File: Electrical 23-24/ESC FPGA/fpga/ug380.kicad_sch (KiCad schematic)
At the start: 0 parts

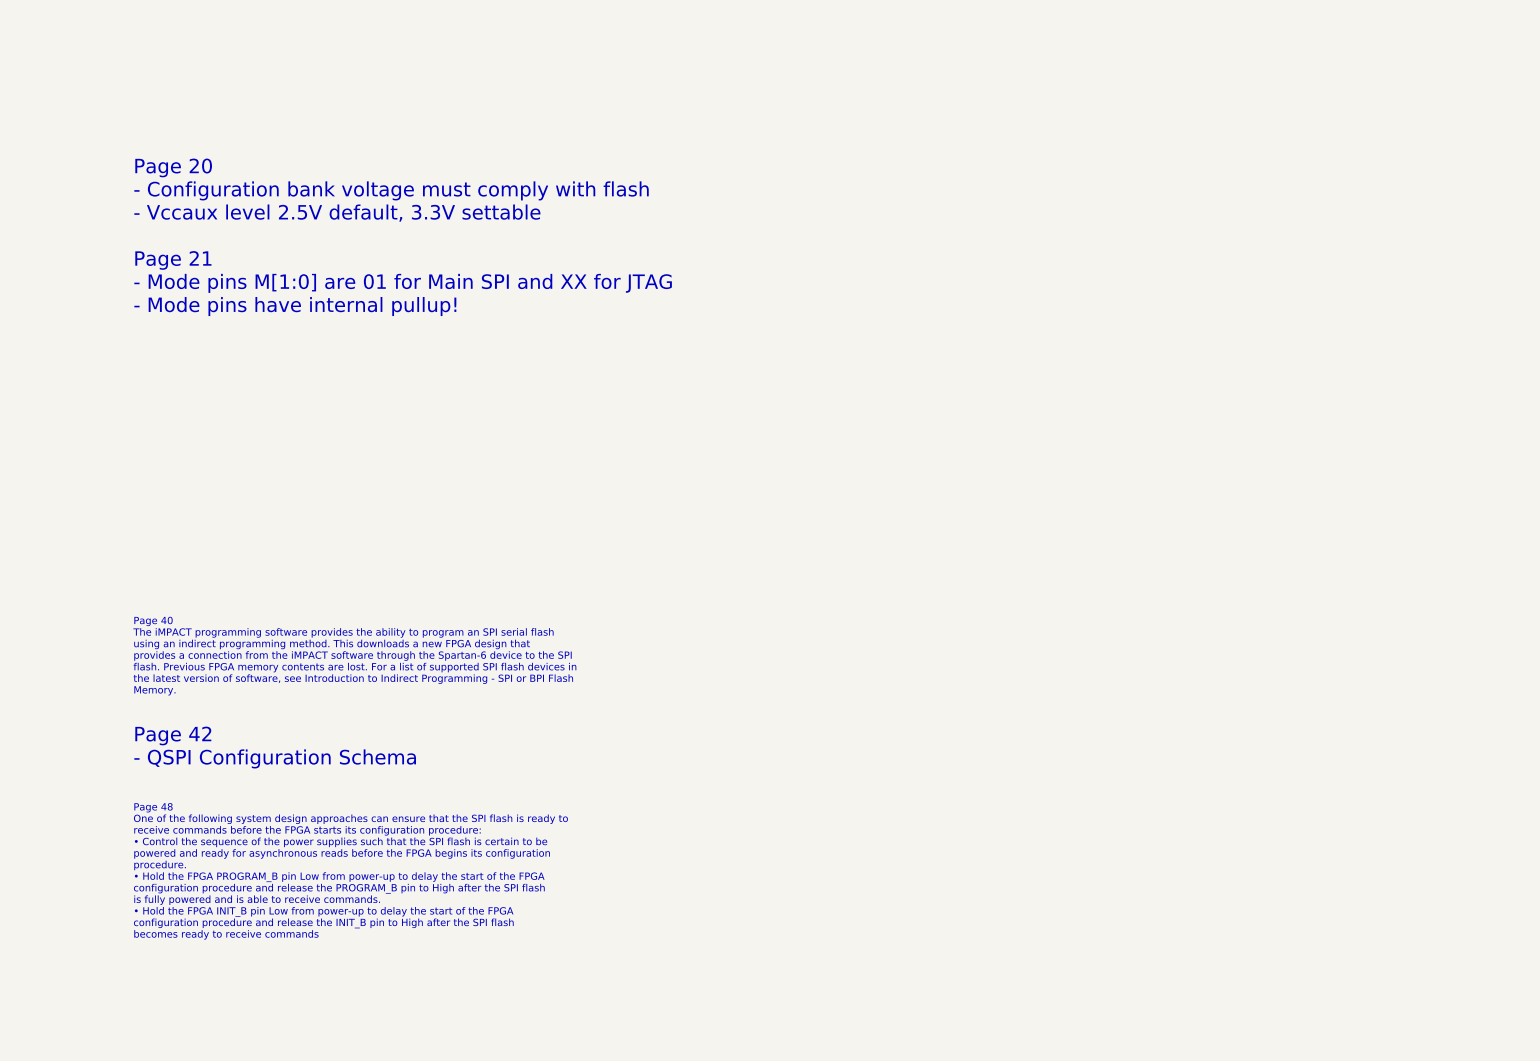
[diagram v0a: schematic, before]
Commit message: Finish programming interface with FPGA
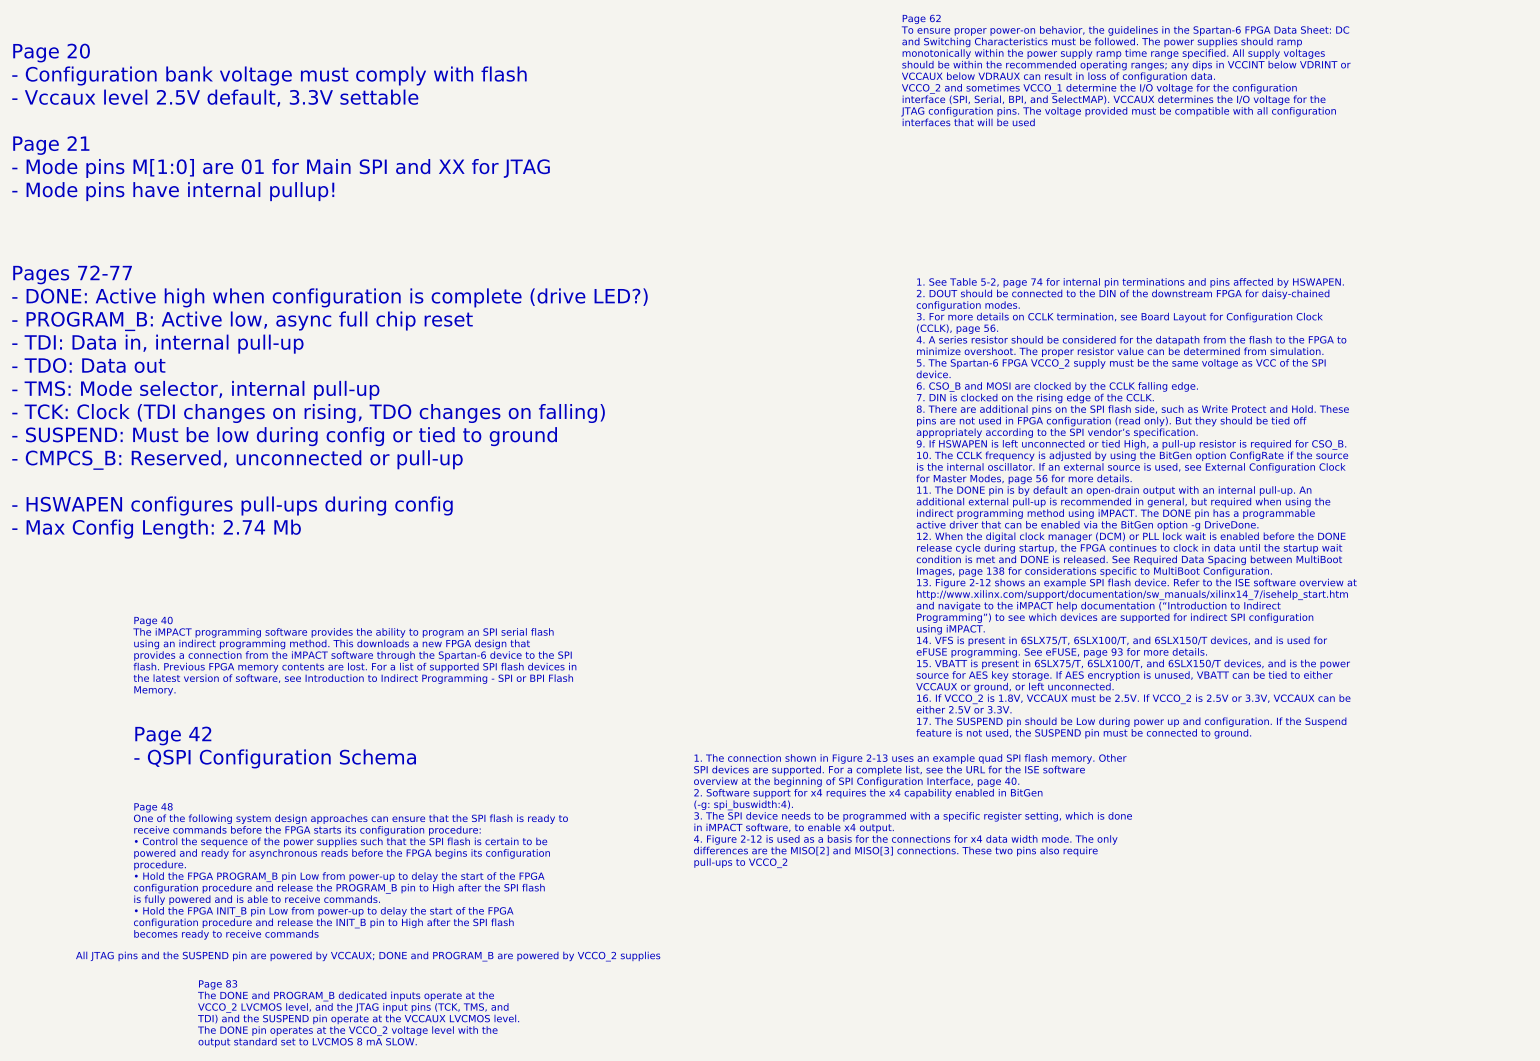
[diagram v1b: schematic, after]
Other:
- note added: "1. See Table 5-2, page 74 for internal pin terminations and pins affected by HSWAPEN. 2. DOUT should be connected to the DIN of the downstream FPGA for daisy-chained configuration modes. 3. For more details on CCLK termination, see Board Layout for Configuration Clock (CCLK), page 56. 4. A series resistor should be considered for the datapath from the flash to the FPGA to minimize overshoot. The 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"
- note added: "1. The connection shown in Figure 2-13 uses an example quad SPI flash memory. Other SPI devices are supported. For a complete list, see the URL for the ISE software overview at the beginning of SPI Configuration Interface, page 40. 2. Software support for x4 requires the x4 capability enabled in BitGen (-g: spi_buswidth:4). 3. The SPI device needs to be programmed with a specific register setting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"
- note added: "All JTAG pins and the SUSPEND pin are powered by VCCAUX; DONE and PROGRAM_B are powered by VCCO_2 supplies"
- note added: "Page 62 To ensure proper power-on behavior, the guidelines in the Spartan-6 FPGA Data Sheet: DC and Switching Characteristics must be followed. The power supplies should ramp monotonically within the power supply ramp time range specified. All supply voltages should be within the recommended operating ranges; any dips in VCCINT below VDRINT or VCCAUX below VDRAUX can result in loss of configurati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"
- note added: "Page 83 The DONE and PROGRAM_B dedicated inputs operate at the VCCO_2 LVCMOS level, and the JTAG input pins (TCK, TMS, and TDI) and the SUSPEND pin operate at the VCCAUX LVCMOS level. The DONE pin operates at the VCCO_2 voltage level with the output standard set to LVCMOS 8 mA SLOW."
- note added: "Pages 72-77 - DONE: Active high when configuration is complete (drive LED?) - PROGRAM_B: Active low, async full chip reset - TDI: Data in, internal pull-up - TDO: Data out - TMS: Mode selector, internal pull-up - TCK: Clock (TDI changes on rising, TDO changes on falling) - SUSPEND: Must be low during config or tied to ground - CMPCS_B: Reserved, unconnected or pull-up - HSWAPEN configures pull-up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"
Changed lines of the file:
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@@
 (kicad_sch (version 20230121) (generator eeschema)
   (paper "A4")
+  (text "Page 62\nTo ensure proper power-on behavior, the guidelines in the Spartan-6 FPGA Data Sheet: DC \nand Switching Characteristics must be followed. The power supplies should ramp \nmonotonically within the power supply ramp time range specified. All supply voltages \nshould be within the recommended operating ranges; any dips in VCCINT below VDRINT or \nVCCAUX below VDRAUX can result in loss of configuration data.\nVCCO_2 and sometimes VCCO_1 determine the I/O voltage for the configuration \ninterface (SPI, Serial, BPI, and SelectMAP). VCCAUX determines the I/O voltage for the \nJTAG configuration pins. The voltage provided must be compatible with all configuration \ninterfaces that will be used"
+    (at 182.88 34.29 0)
+    (effects (font (size 1.27 1.27)) (justify left bottom))
+  )
   (text "Page 20\n- Configuration bank voltage must comply with flash\n- Vccaux level 2.5V default, 3.3V settable\n\nPage 21\n- Mode pins M[1:0] are 01 for Main SPI and XX for JTAG\n- Mode pins have internal pullup!"
-    (at 46.99 67.31 0)
+    (at 25.4 46.99 0)
     (effects (font (size 2.54 2.54)) (justify left bottom))
   )
+  (text "1. The connection shown in Figure 2-13 uses an example quad SPI flash memory. Other \nSPI devices are supported. For a complete list, see the URL for the ISE software \noverview at the beginning of SPI Configuration Interface, page 40.\n2. Software support for x4 requires the x4 capability enabled in BitGen \n(-g: spi_buswidth:4).\n3. The SPI device needs to be programmed with a specific register setting, which is done \nin iMPACT software, to enable x4 output.\n4. Figure 2-12 is used as a basis for the connections for x4 data width mode. The only \ndifferences are the MISO[2] and MISO[3] connections. These two pins also require \npull-ups to VCCO_2"
+    (at 146.05 165.1 0)
+    (effects (font (size 1.27 1.27)) (justify left bottom))
+  )
   (text "Page 42\n- QSPI Configuration Schema" (at 46.99 147.32 0)
+    (effects (font (size 2.54 2.54)) (justify left bottom))
+  )
+  (text "Pages 72-77\n- DONE: Active high when configuration is complete (drive LED?)\n- PROGRAM_B: Active low, async full chip reset\n- TDI: Data in, internal pull-up\n- TDO: Data out\n- TMS: Mode selector, internal pull-up\n- TCK: Clock (TDI changes on rising, TDO changes on falling)\n- SUSPEND: Must be low during config or tied to ground\n- CMPCS_B: Reserved, unconnected or pull-up\n\n- HSWAPEN configures pull-ups during config\n- Max Config Length: 2.74 Mb"
+    (at 25.4 106.68 0)
     (effects (font (size 2.54 2.54)) (justify left bottom))
   )
@@
     (effects (font (size 1.27 1.27)) (justify left bottom))
   )
+  (text "Page 83\nThe DONE and PROGRAM_B dedicated inputs operate at the\nVCCO_2 LVCMOS level, and the JTAG input pins (TCK, TMS, and \nTDI) and the SUSPEND pin operate at the VCCAUX LVCMOS level. \nThe DONE pin operates at the VCCO_2 voltage level with the \noutput standard set to LVCMOS 8 mA SLOW."
+    (at 58.42 196.85 0)
+    (effects (font (size 1.27 1.27)) (justify left bottom))
+  )
+  (text "1. See Table 5-2, page 74 for internal pin terminations and pins affected by HSWAPEN.\n2. DOUT should be connected to the DIN of the downstream FPGA for daisy-chained \nconfiguration modes.\n3. For more details on CCLK termination, see Board Layout for Configuration Clock \n(CCLK), page 56.\n4. A series resistor should be considered for the datapath from the flash to the FPGA to \nminimize overshoot. The proper resistor value can be determined from simulation.\n5. The Spartan-6 FPGA VCCO_2 supply must be the same voltage as VCC of the SPI \ndevice.\n6. CSO_B and MOSI are clocked by the CCLK falling edge.\n7. DIN is clocked on the rising edge of the CCLK.\n8. There are additional pins on the SPI flash side, such as Write Protect and Hold. These \npins are not used in FPGA configuration (read only). But they should be tied off \nappropriately according to the SPI vendor’s specification. \n9. If HSWAPEN is left unconnected or tied High, a pull-up resistor is required for CSO_B.\n10. The CCLK frequency is adjusted by using the BitGen option ConfigRate if the source \nis the internal oscillator. If an external source is used, see External Configuration Clock \nfor Master Modes, page 56 for more details.\n11. The DONE pin is by default an open-drain output with an internal pull-up. An \nadditional external pull-up is recommended in general, but required when using the \nindirect programming method using iMPACT. The DONE pin has a programmable \nactive driver that can be enabled via the BitGen option -g DriveDone.\n12. When the digital clock manager (DCM) or PLL lock wait is enabled before the DONE \nrelease cycle during startup, the FPGA continues to clock in data until the startup wait \ncondition is met and DONE is released. See Required Data Spacing between MultiBoot \nImages, page 138 for considerations specific to MultiBoot Configuration.\n13. Figure 2-12 shows an example SPI flash device. Refer to the ISE software overview at \nhttp://www.xilinx.com/support/documentation/sw_manuals/xilinx14_7/isehelp_start.htm\nand navigate to the iMPACT help documentation (“Introduction to Indirect \nProgramming”) to see which devices are supported for indirect SPI configuration \nusing iMPACT.\n14. VFS is present in 6SLX75/T, 6SLX100/T, and 6SLX150/T devices, and is used for \neFUSE programming. See eFUSE, page 93 for more details.\n15. VBATT is present in 6SLX75/T, 6SLX100/T, and 6SLX150/T devices, and is the power \nsource for AES key storage. If AES encryption is unused, VBATT can be tied to either \nVCCAUX or ground, or left unconnected.\n16. If VCCO_2 is 1.8V, VCCAUX must be 2.5V. If VCCO_2 is 2.5V or 3.3V, VCCAUX can be \neither 2.5V or 3.3V.\n17. The SUSPEND pin should be Low during power up and configuration. If the Suspend \nfeature is not used, the SUSPEND pin must be connected to ground."
+    (at 185.42 142.24 0)
+    (effects (font (size 1.27 1.27)) (justify left bottom))
+  )
   (text "Page 40\nThe iMPACT programming software provides the ability to program an SPI serial flash \nusing an indirect programming method. This downloads a new FPGA design that \nprovides a connection from the iMPACT software through the Spartan-6 device to the SPI \nflash. Previous FPGA memory contents are lost. For a list of supported SPI flash devices in \nthe latest version of software, see Introduction to Indirect Programming - SPI or BPI Flash \nMemory."
     (at 46.99 134.62 0)
     (effects (font (size 1.27 1.27)) (justify left bottom))
   )
+  (text "All JTAG pins and the SUSPEND pin are powered by VCCAUX; DONE and PROGRAM_B are powered by VCCO_2 supplies"
+    (at 36.83 181.61 0)
+    (effects (font (size 1.27 1.27)) (justify left bottom))
+  )

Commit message: Working on FPGA board
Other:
- note added: "oscillator goes on gclk0_userclk"
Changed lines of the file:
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@@
+    (effects (font (size 1.27 1.27)) (justify left bottom))
+  )
+  (text "oscillator goes on gclk0_userclk" (at 139.7 111.76 0)
     (effects (font (size 1.27 1.27)) (justify left bottom))
   )
